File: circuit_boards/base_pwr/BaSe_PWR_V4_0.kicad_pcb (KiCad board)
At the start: 2 copper layers, 114.2 x 103.5 mm, 101 parts, among them J1 12VDC In, J10 Conn_01x04_Socket, J11 MOTOR, J12 USB3_A, J3 USB_B_Micro, J4 Conn_01x07_Pin, J5 Conn_02x06_Odd_Even, J6 USB3_B_Micro, J7 Conn_02x06_Odd_Even, J8 USB_C_Receptacle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

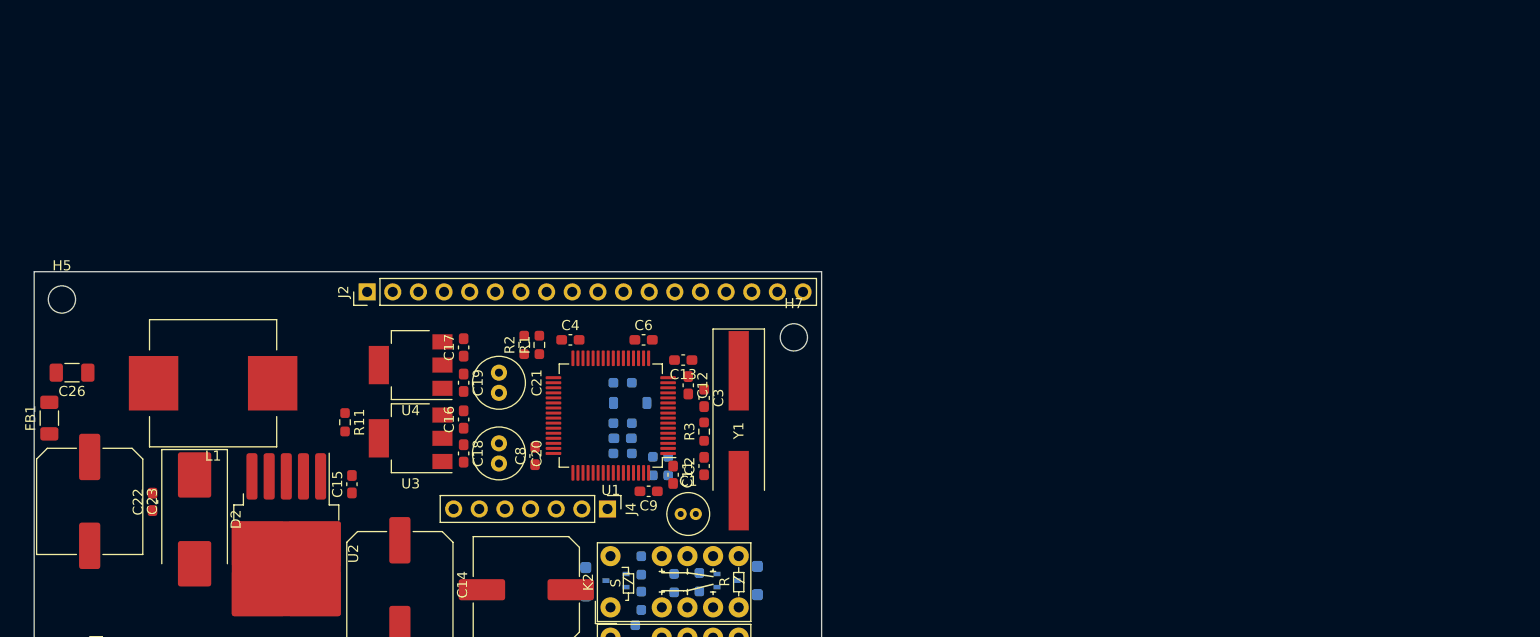
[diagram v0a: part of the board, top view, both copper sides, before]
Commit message: BaSe PWR V4.0: add endwitch
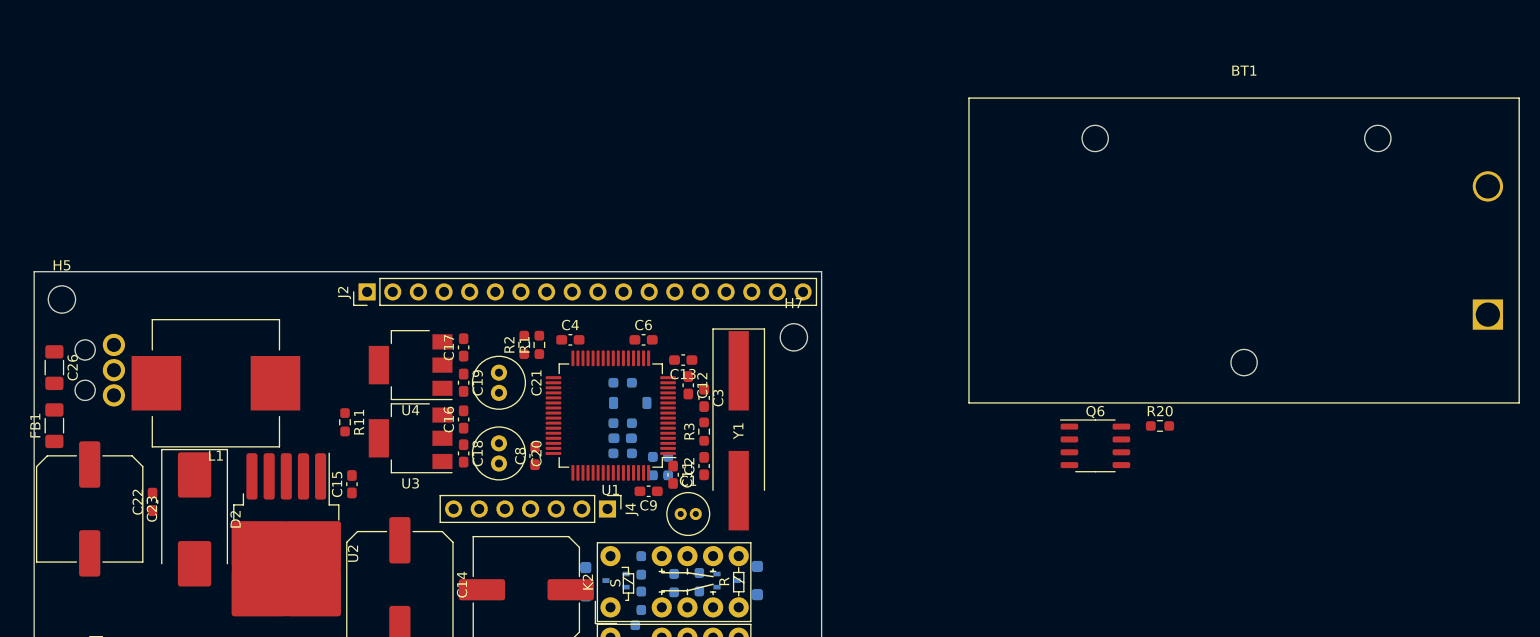
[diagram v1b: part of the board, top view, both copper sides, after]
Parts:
- added BT1: Battery, Battery:BatteryHolder_Eagle_12BH611-GR, F.Cu at (164.0, 67.8)
- added Q6: AOSP21321, Package_SO:SO-8_3.9x4.9mm_P1.27mm, F.Cu at (125.1, 80.8)
- added R20: 100k, Resistor_SMD:R_0603_1608Metric_Pad0.98x0.95mm_HandSolder, F.Cu at (131.5, 78.8)
- added U6: TS0101F020V4, g7_switch:TS0101F020V4, B.Cu at (27.9, 73.2)
- moved C26 1.82 mm to (22.0, 73.0), turned to -90 degrees
- moved FB1 0.90 mm to (22.0, 78.8)
- moved C23 0.75 mm to (25.5, 87.0)
- moved L1 0.27 mm to (38.0, 74.5)
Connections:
- R9 pad 1: +12V -> /12V_nProt
- U1 pad 28: unconnected-(U1-PB2-Pad28) -> /~{endswitch_undocked}
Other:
- copper layers 2 -> 4
- board text added: "0"
- board text added: "0 mm"
- board text added: "0,01 mm"
- board text added: "0,02"
- board text added: "0,035 mm"
- board text added: "0,1 mm"
- board text added: "1"
- board text added: "1,64 mm"
- board text added: "3,3"
- board text added: "4,5"
- board text added: "B.Cu"
- board text added: "B.Mask"
- board text added: "B.Paste"
- board text added: "B.Silkscreen"
- board text added: "Bottom Silk Screen"
- board text added: "Bottom Solder Mask"
- board text added: "Bottom Solder Paste"
- board text added: "Color"
- board text added: "Dielectric 1"
- board text added: "Dielectric 2"
- board text added: "Dielectric 3"
- board text added: "Epsilon R"
- board text added: "F.Cu"
- board text added: "F.Mask"
- board text added: "F.Paste"
- board text added: "F.Silkscreen"
- board text added: "FR4"
- board text added: "In1.Cu"
- board text added: "In2.Cu"
- board text added: "Layer Name"
- board text added: "Loss Tangent"
- board text added: "Material"
- board text added: "Not specified"
- board text added: "Thickness (mm)"
- board text added: "Top Silk Screen"
- board text added: "Top Solder Mask"
- board text added: "Top Solder Paste"
- board text added: "Type"
- board text added: "copper"
- board text added: "core"
- board text added: "prepreg"

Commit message: BaSe PWR V4.0: add 3d models, define layer stackup
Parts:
- removed BT1: Battery, Battery:BatteryHolder_Eagle_12BH611-GR
- removed Q6: AOSP21321, Package_SO:SO-8_3.9x4.9mm_P1.27mm
- removed R20: 100k, Resistor_SMD:R_0603_1608Metric_Pad0.98x0.95mm_HandSolder
- C26, FB1: moved to B.Cu
- J3: footprint Connector_USB:USB_Micro-B_Molex-105017-0001 -> g7_connectors:USB_Micro-B_Molex-105017-0001
- L1: footprint Inductor_SMD:L_Wuerth_WE-PD-Typ-LS_Handsoldering -> g7_inductor:L_Wuerth_WE-PD-Typ-LS_Handsoldering
- moved C26 18.0 mm to (31.5, 88.2), turned to 90 degrees
- moved FB1 9.43 mm to (27.0, 86.8), turned to 0 degrees
- moved C14 1.69 mm to (57.0, 96.0)
- moved C24 1.03 mm to (69.0, 96.0), turned to -90 degrees
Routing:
- net /stator_tx-: track 27.7 -> 0.00 mm, vias 1 -> 0
- net /stator_tx+: track 27.7 -> 0.00 mm, vias 1 -> 0
- net /stator_d+: track 31.9 -> 32.9 mm
- net /stator_d-: track 31.9 -> 32.9 mm

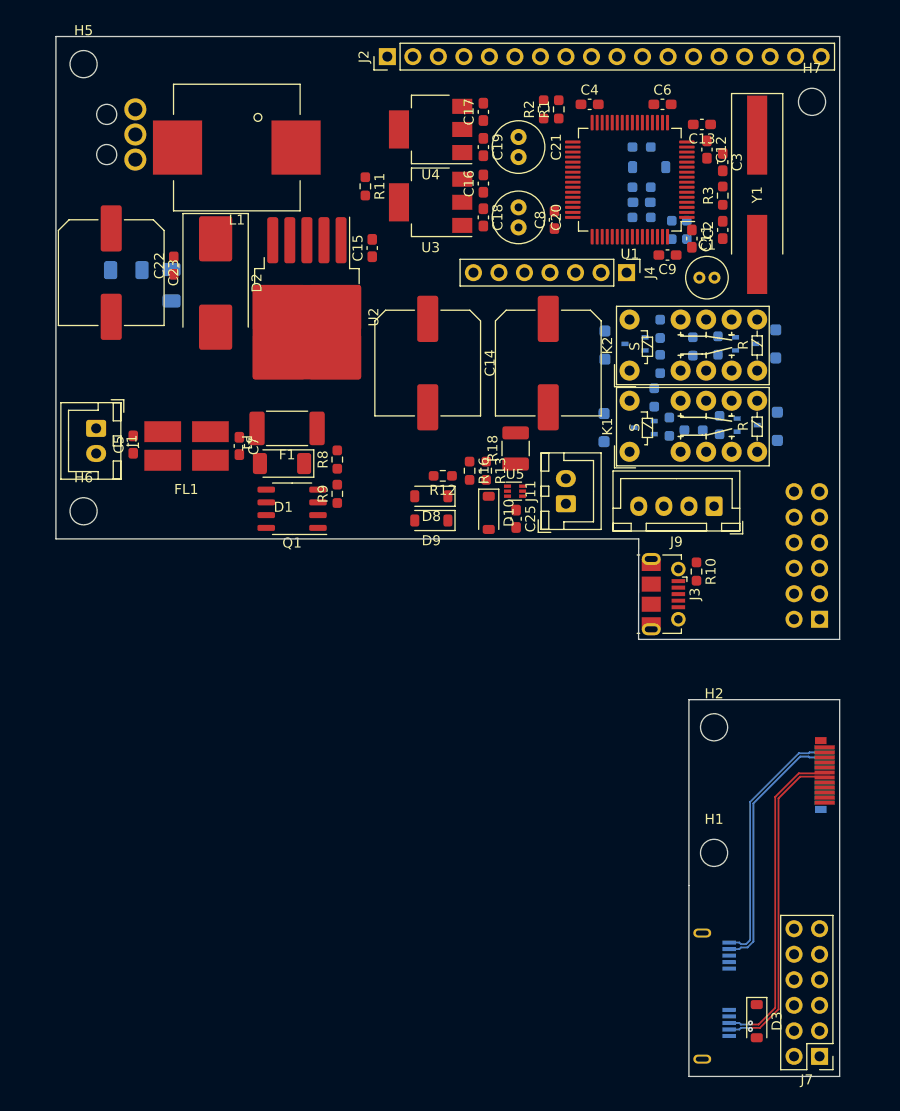
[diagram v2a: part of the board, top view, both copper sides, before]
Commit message: BaSe PWR V4.0: push to MCAD. Moved some stuff.
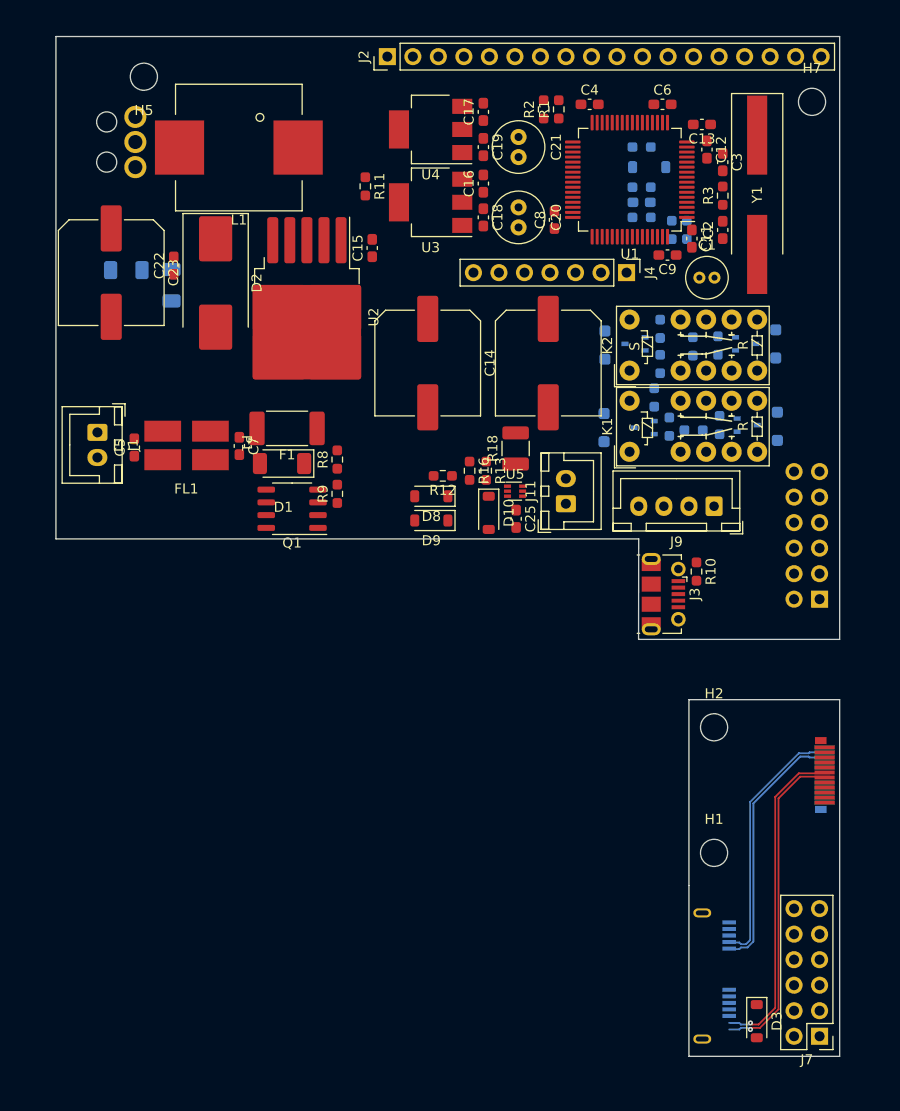
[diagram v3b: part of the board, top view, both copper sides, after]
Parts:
- removed H6: MountingHole, MountingHole:MountingHole_2.7mm_M2.5_DIN965
- moved H5 6.13 mm to (28.8, 67.5), turned to 180 degrees
- moved J5 2.00 mm to (96.0, 119.5)
- moved J6 2.00 mm to (84.3, 157.0)
- moved J7 2.00 mm to (96.0, 163.0)
- moved U6 0.75 mm to (27.9, 74.0)
- moved J1 0.42 mm to (24.1, 102.9)
- moved C5 0.31 mm to (27.8, 104.4)
- moved L1 0.20 mm to (38.2, 74.5)
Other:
- board size 114.2 x 103.5 mm -> 114.2 x 101.5 mm
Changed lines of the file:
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@@
   )
   (footprint "Connector_PinHeader_2.54mm:PinHeader_2x06_P2.54mm_Vertical" (layer "F.Cu")
-    (at 96 165 180)
+    (at 96 163 180)
     (descr "Through hole straight pin header, 2x06, 2.54mm pitch, double rows")
     (tags "Through hole pin header THT 2x06 2.54mm double row")
@@
   )
   (footprint "Capacitor_SMD:C_0603_1608Metric_Pad1.08x0.95mm_HandSolder" (layer "F.Cu")
-    (at 27.689655 104.1125 90)
+    (at 27.8 104.4 90)
     (descr "Capacitor SMD 0603 (1608 Metric), square (rectangular) end terminal, IPC_7351 nominal with elongated pad for handsoldering. (Body size source: IPC-SM-782 page 76, https://www.pcb-3d.com/wordpress/wp-content/uploads/ipc-sm-782a_amendment_1_and_2.pdf), generated with kicad-footprint-generator")
     (tags "capacitor handsolder")
@@
   )
   (footprint "Connector_JST:JST_XH_B2B-XH-A_1x02_P2.50mm_Vertical" (layer "F.Cu")
-    (at 24 102.5 -90)
+    (at 24.125 102.9 -90)
     (descr "JST XH series connector, B2B-XH-A (http://www.jst-mfg.com/product/pdf/eng/eXH.pdf), generated with kicad-footprint-generator")
     (tags "connector JST XH vertical")
@@
   )
   (footprint "g7_inductor:L_Wuerth_WE-PD-Typ-LS_Handsoldering" (layer "F.Cu")
-    (at 38 74.55 180)
+    (at 38.2 74.55 180)
     (descr "Shielded Power Inductor, Wuerth Elektronik, WE-PD, SMD, Typ LS, Handsoldering, https://katalog.we-online.com/pbs/datasheet/7447715906.pdf")
     (tags "Choke Shielded Power Inductor WE-PD TypLS Wuerth")
@@
   )
   (footprint "MountingHole:MountingHole_2.7mm_M2.5_DIN965" (layer "F.Cu")
-    (at 22.75 66.25)
+    (at 28.75 67.5 180)
     (descr "Mounting Hole 2.7mm, no annular, M2.5, DIN965")
     (tags "mounting hole 2.7mm no annular m2.5 din965")
@@
     (fp_circle (center 0 0) (end 2.6 0)
       (stroke (width 0.05) (type solid)) (fill none) (layer "F.CrtYd"))
-    (pad "" np_thru_hole circle (at 0 0) (size 2.7 2.7) (drill 2.7) (layers "*.Cu" "*.Mask"))
+    (pad "" np_thru_hole circle (at 0 0 180) (size 2.7 2.7) (drill 2.7) (layers "*.Cu" "*.Mask"))
   )
   (footprint "Capacitor_SMD:C_0603_1608Metric_Pad1.08x0.95mm_HandSolder" (layer "F.Cu")
@@
     )
   )
-  (footprint "MountingHole:MountingHole_2.7mm_M2.5_DIN965" (layer "F.Cu")
-    (at 22.75 110.75)
-    (descr "Mounting Hole 2.7mm, no annular, M2.5, DIN965")
-    (tags "mounting hole 2.7mm no annular m2.5 din965")
-    (property "Sheetfile" "BaSe_PWR_V4_0.kicad_sch")
-    (property "Sheetname" "")
-    (property "ki_description" "Mounting Hole without connection")
-    (property "ki_keywords" "mounting hole")
-    (attr exclude_from_pos_files)
-    (fp_text reference "H6" (at 0 -3.35) (layer "F.SilkS")
-        (effects (font (size 1 1) (thickness 0.15)))
-    )
-    (fp_text value "MountingHole" (at 0 3.35) (layer "F.Fab")
-        (effects (font (size 1 1) (thickness 0.15)))
-    )
-    (fp_text user "${REFERENCE}" (at 0 0) (layer "F.Fab")
-        (effects (font (size 1 1) (thickness 0.15)))
-    )
-    (fp_circle (center 0 0) (end 2.35 0)
-      (stroke (width 0.15) (type solid)) (fill none) (layer "Cmts.User"))
-    (fp_circle (center 0 0) (end 2.6 0)
-      (stroke (width 0.05) (type solid)) (fill none) (layer "F.CrtYd"))
-    (pad "" np_thru_hole circle (at 0 0) (size 2.7 2.7) (drill 2.7) (layers "*.Cu" "*.Mask"))
-  )
   (footprint "Connector_JST:JST_XH_B2B-XH-A_1x02_P2.50mm_Vertical" (layer "F.Cu")
     (at 70.75 110 90)
@@
   )
   (footprint "g7_emi:CMC_Laird_CM2021Y330R-10" (layer "F.Cu")
-    (at 33 104.25)
+    (at 33 104.2)
     (property "SPN" "240-2502-1-ND")
     (property "Sheetfile" "BaSe_PWR_V4_0.kicad_sch")
@@
   )
   (footprint "g7_switch:TS0101F020V4" (layer "B.Cu")
-    (at 27.9 73.25 -90)
+    (at 27.9 74 -90)
     (property "Digikey" "EG4938-ND")
     (property "Sheetfile" "BaSe_PWR_V4_0.kicad_sch")
@@
   )
   (footprint "Connector_PinSocket_2.54mm:PinSocket_2x06_P2.54mm_Vertical" (layer "B.Cu")
-    (at 96 121.5)
+    (at 96 119.5)
     (descr "Through hole straight socket strip, 2x06, 2.54mm pitch, double cols (from Kicad 4.0.7), script generated")
     (tags "Through hole socket strip THT 2x06 2.54mm double row")
@@
   )
   (footprint "g7_connectors:conn_usb3bmicro_GSB343K331HR" (layer "B.Cu")
-    (at 84.325 159 90)
+    (at 84.325 157 90)
     (property "Digikey" "664-GSB343K331HRCT-ND")
     (property "MPN" "GSB343K331HR")
@@
   (gr_line (start 112.25 149) (end 134.25 149)
     (stroke (width 0.1) (type default)) (layer "Edge.Cuts"))
-  (gr_line (start 83 148) (end 83 167)
+  (gr_line (start 83 148) (end 83 165)
     (stroke (width 0.1) (type default)) (layer "Edge.Cuts"))
-  (gr_line (start 83 167) (end 98 167)
+  (gr_line (start 83 165) (end 98 165)
     (stroke (width 0.1) (type default)) (layer "Edge.Cuts"))
   (gr_line (start 77.984 123.5) (end 78 113.5)
@@
   (gr_line (start 134.25 125) (end 112.25 125)
     (stroke (width 0.1) (type default)) (layer "Edge.Cuts"))
-  (gr_line (start 98 167) (end 98 129.5)
+  (gr_line (start 98 165) (end 98 129.5)
     (stroke (width 0.1) (type default)) (layer "Edge.Cuts"))
   (gr_line (start 77.984 123.5) (end 98 123.5)
@@
       (effects (font (size 1 1) (thickness 0.15)))
     )
+    (format (prefix "") (suffix "") (units 3) (units_format 1) (precision 4))
+    (style (thickness 0.15) (arrow_length 1.27) (text_position_mode 0) (extension_height 0.58642) (extension_offset 0.5) keep_text_aligned)
+  )
+  (dimension (type aligned) (layer "User.1")
+    (pts (xy 83 167) (xy 98 167))
+    (height 10.2)
+    (gr_text "15,0000 mm" (at 90.5 176.05) (layer "User.1")
+      (effects (font (size 1 1) (thickness 0.15)))
+    )
